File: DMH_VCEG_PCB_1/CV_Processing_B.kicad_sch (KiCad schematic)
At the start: 58 parts, among them J26 Conn_01x10_PinHeader, Q27 BC558, Q28 BC558, Q29 BC548, Q30 BC548, Q31 BC548, Q32 BC548, U18 TL074, U19 TL074, U20 TL074

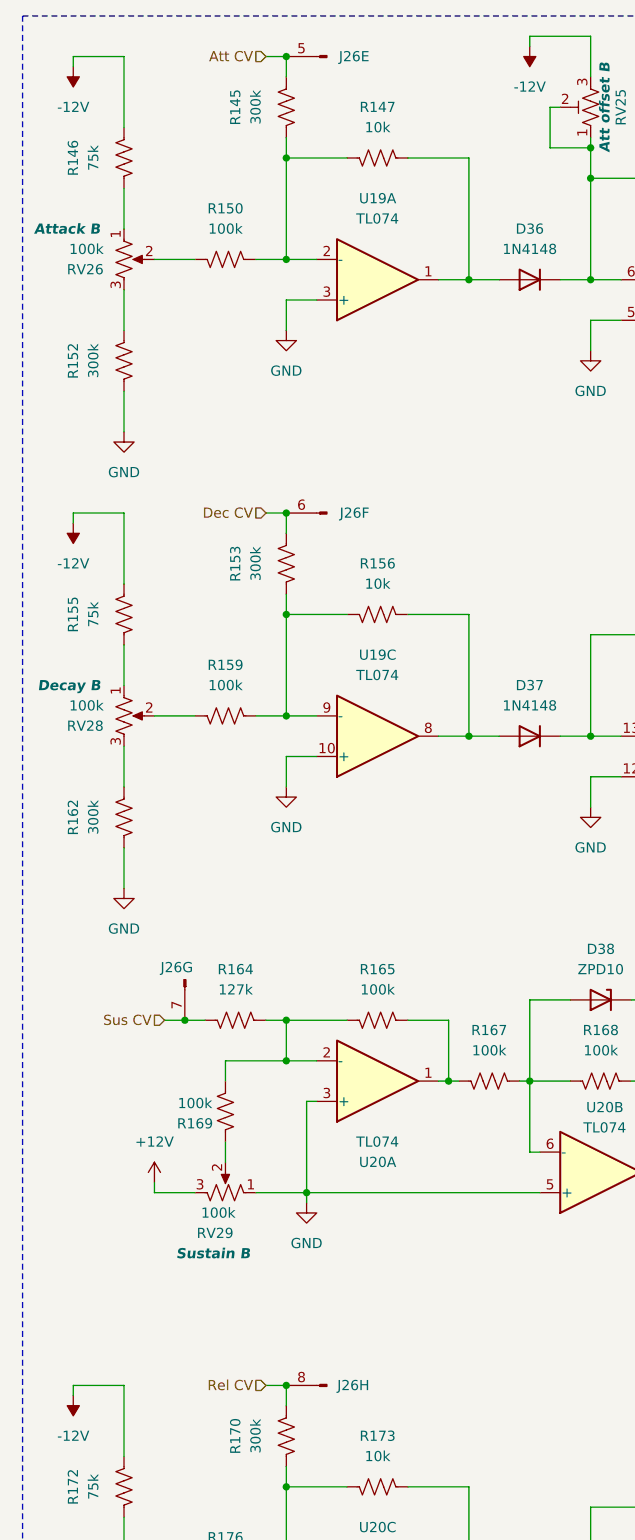
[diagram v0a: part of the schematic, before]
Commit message: PCB 2 placement in progress
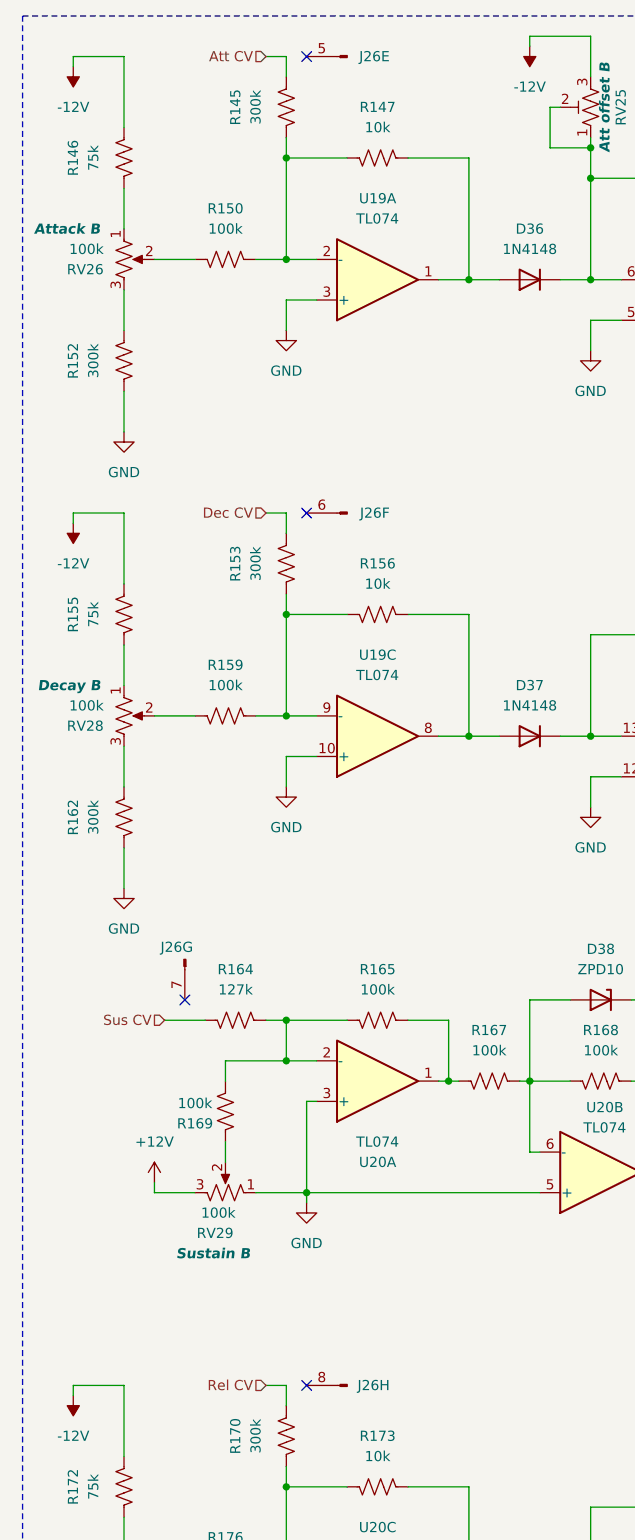
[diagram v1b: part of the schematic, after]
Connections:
- net Att CV: no longer J26.5 (Pin_5)
- net Dec CV: no longer J26.6 (Pin_6)
- net Rel CV: no longer J26.8 (Pin_8)
- net Sus CV: no longer J26.7 (Pin_7)
- no-connect marks 0 -> 4

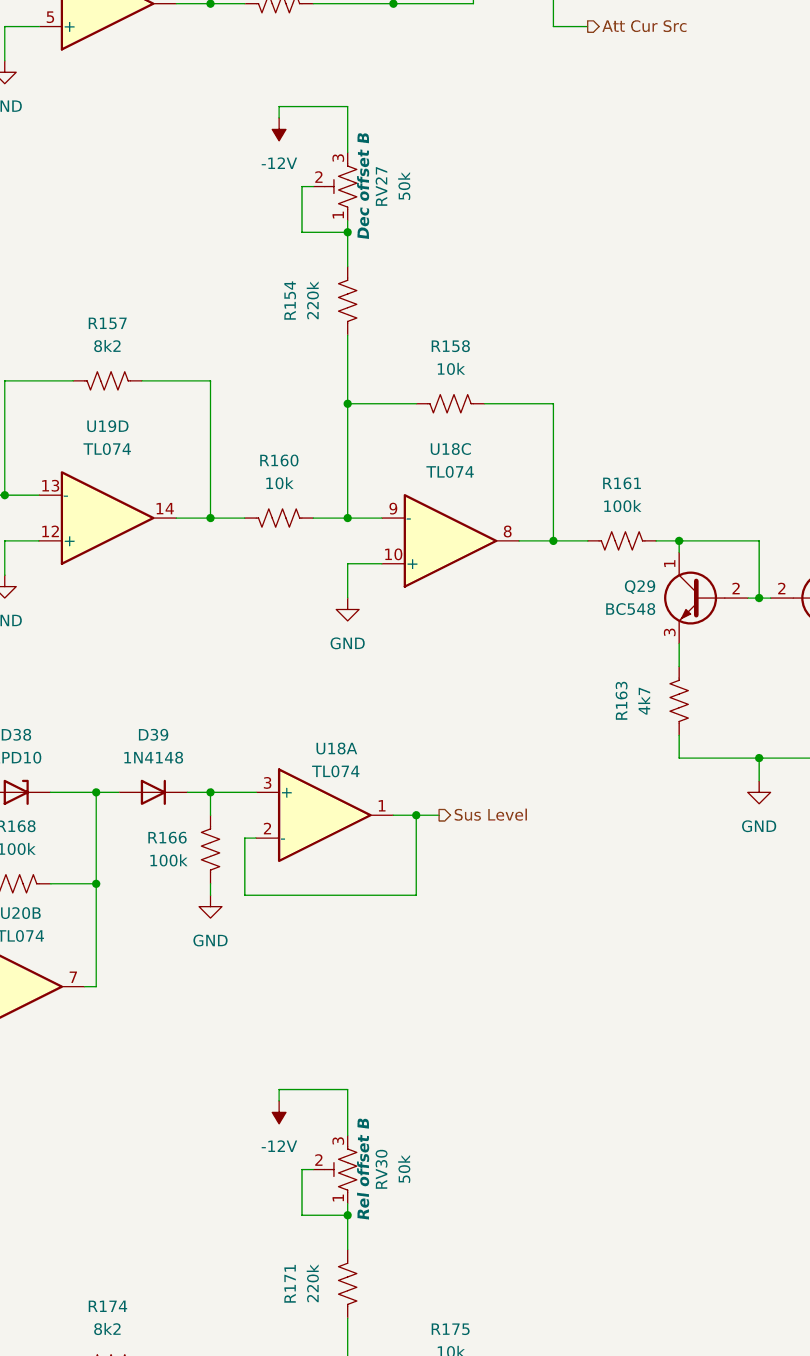
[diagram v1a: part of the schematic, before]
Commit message: Updated Dec and Rel trimpots to 100k
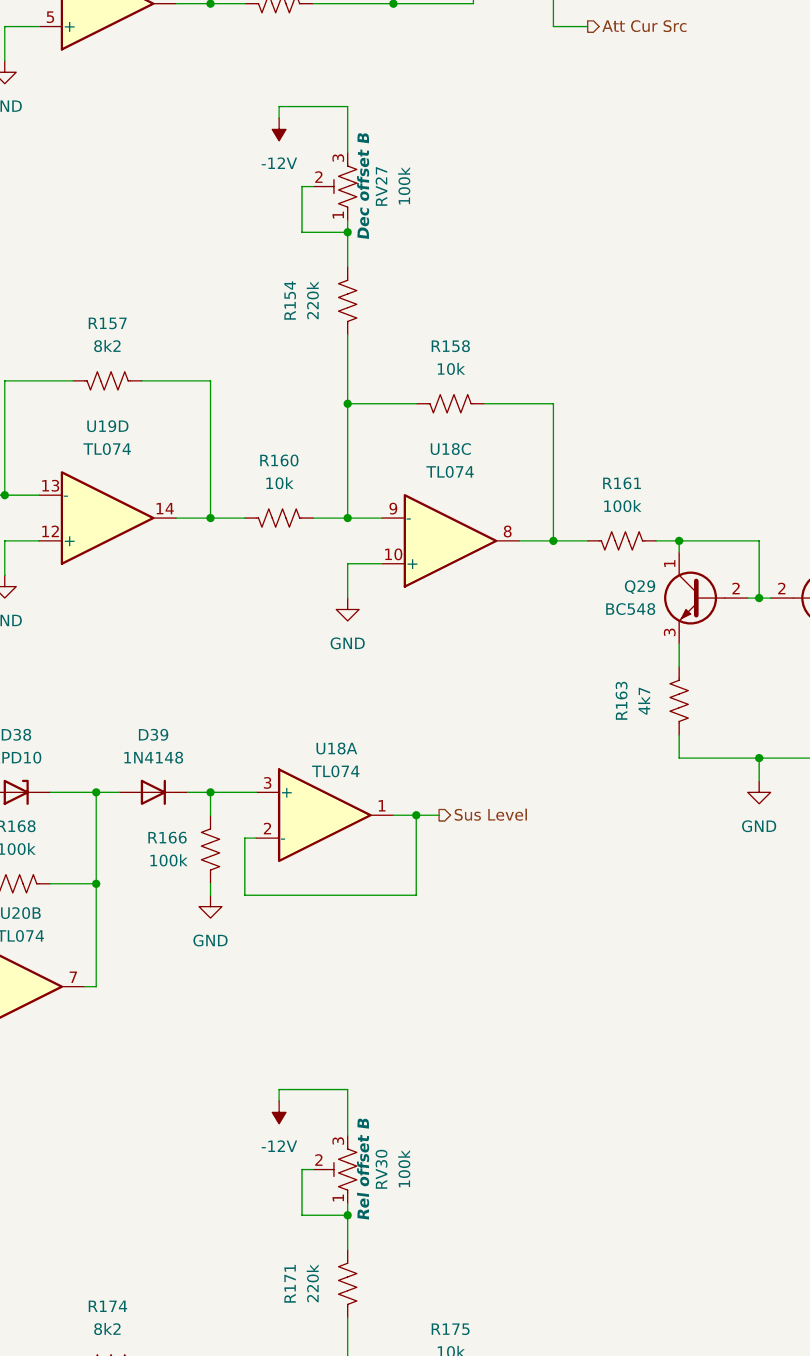
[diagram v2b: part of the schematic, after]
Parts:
- RV27, RV30: value 50k -> 100k
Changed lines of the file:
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@@
 			)
 		)
-		(property "Value" "50k"
+		(property "Value" "100k"
 			(at 128.27 69.85 90)
 			(effects
@@
 			)
 		)
-		(property "Value" "50k"
+		(property "Value" "100k"
 			(at 128.27 179.07 90)
 			(effects

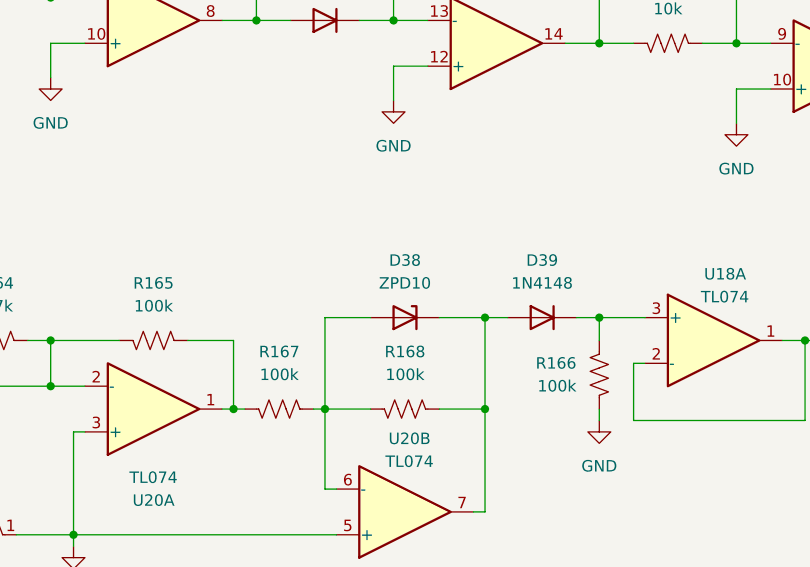
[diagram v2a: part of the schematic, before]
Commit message: PCB 2 placement ongoing
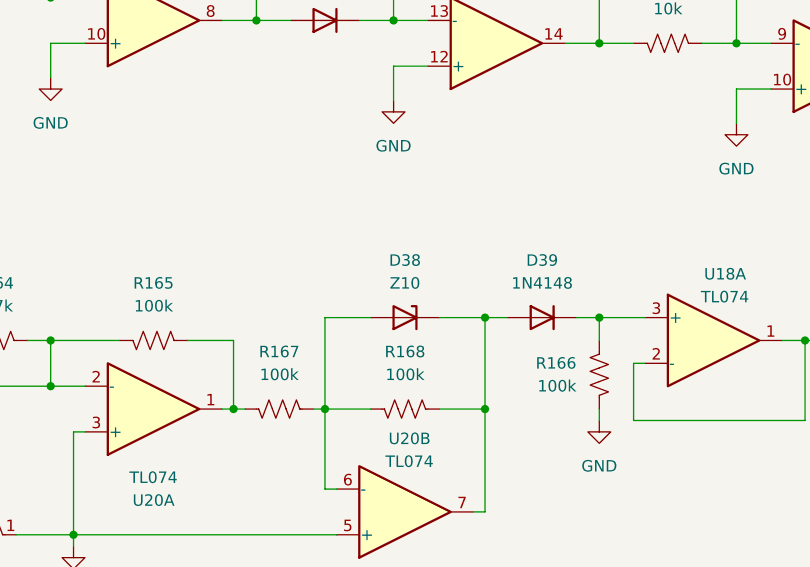
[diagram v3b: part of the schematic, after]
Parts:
- D38: value ZPD10 -> Z10
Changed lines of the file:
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@@
 			)
 		)
-		(property "Value" "ZPD10"
+		(property "Value" "Z10"
 			(at 85.09 133.35 0)
 			(effects

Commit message: PCB 2 routing in progress
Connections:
- net Att CV: now also J26.5 (Pin_5)
- net Dec CV: now also J26.6 (Pin_6)
- net Rel CV: now also J26.8 (Pin_8)
- net Sus CV: now also J26.7 (Pin_7)
- no-connect marks 4 -> 0
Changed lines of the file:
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@@
+	)
+	(junction
+		(at 45.72 76.2)
+		(diameter 0)
+		(color 0 0 0 0)
 	)
 	(junction
@@
 	)
 	(junction
+		(at 45.72 19.05)
+		(diameter 0)
+		(color 0 0 0 0)
+	)
+	(junction
 		(at 121.92 215.9)
 		(diameter 0)
@@
 	)
 	(junction
+		(at 33.02 139.7)
+		(diameter 0)
+		(color 0 0 0 0)
+	)
+	(junction
 		(at 106.68 137.16)
 		(diameter 0)
@@
 	)
 	(junction
+		(at 45.72 185.42)
+		(diameter 0)
+		(color 0 0 0 0)
+	)
+	(junction
 		(at 127 49.53)
 		(diameter 0)
@@
 		(color 0 0 0 0)
 	)
-	(no_connect
-		(at 48.26 185.42)
-	)
-	(no_connect
-		(at 48.26 76.2)
-	)
-	(no_connect
-		(at 33.02 137.16)
-	)
-	(no_connect
-		(at 48.26 19.05)
-	)
 	(wire
 		(pts
@@
 	(wire
 		(pts
-			(xy 30.48 139.7) (xy 35.56 139.7)
+			(xy 30.48 139.7) (xy 33.02 139.7)
 		)
 		(stroke
@@
 	(wire
 		(pts
+			(xy 45.72 19.05) (xy 48.26 19.05)
+		)
+		(stroke
+			(width 0)
+			(type default)
+		)
+	)
+	(wire
+		(pts
 			(xy 121.92 170.18) (xy 121.92 175.26)
 		)
@@
 	(wire
 		(pts
+			(xy 33.02 137.16) (xy 33.02 139.7)
+		)
+		(stroke
+			(width 0)
+			(type default)
+		)
+	)
+	(wire
+		(pts
 			(xy 102.87 215.9) (xy 106.68 215.9)
 		)
@@
 	(wire
 		(pts
+			(xy 45.72 185.42) (xy 48.26 185.42)
+		)
+		(stroke
+			(width 0)
+			(type default)
+		)
+	)
+	(wire
+		(pts
 			(xy 176.53 120.65) (xy 176.53 133.35)
 		)
@@
 	(wire
 		(pts
+			(xy 45.72 76.2) (xy 48.26 76.2)
+		)
+		(stroke
+			(width 0)
+			(type default)
+		)
+	)
+	(wire
+		(pts
 			(xy 80.01 104.14) (xy 83.82 104.14)
 		)
@@
 		)
 		(stroke
+			(width 0)
+			(type default)
+		)
+	)
+	(wire
+		(pts
+			(xy 33.02 139.7) (xy 35.56 139.7)
+		)
+		(stroke

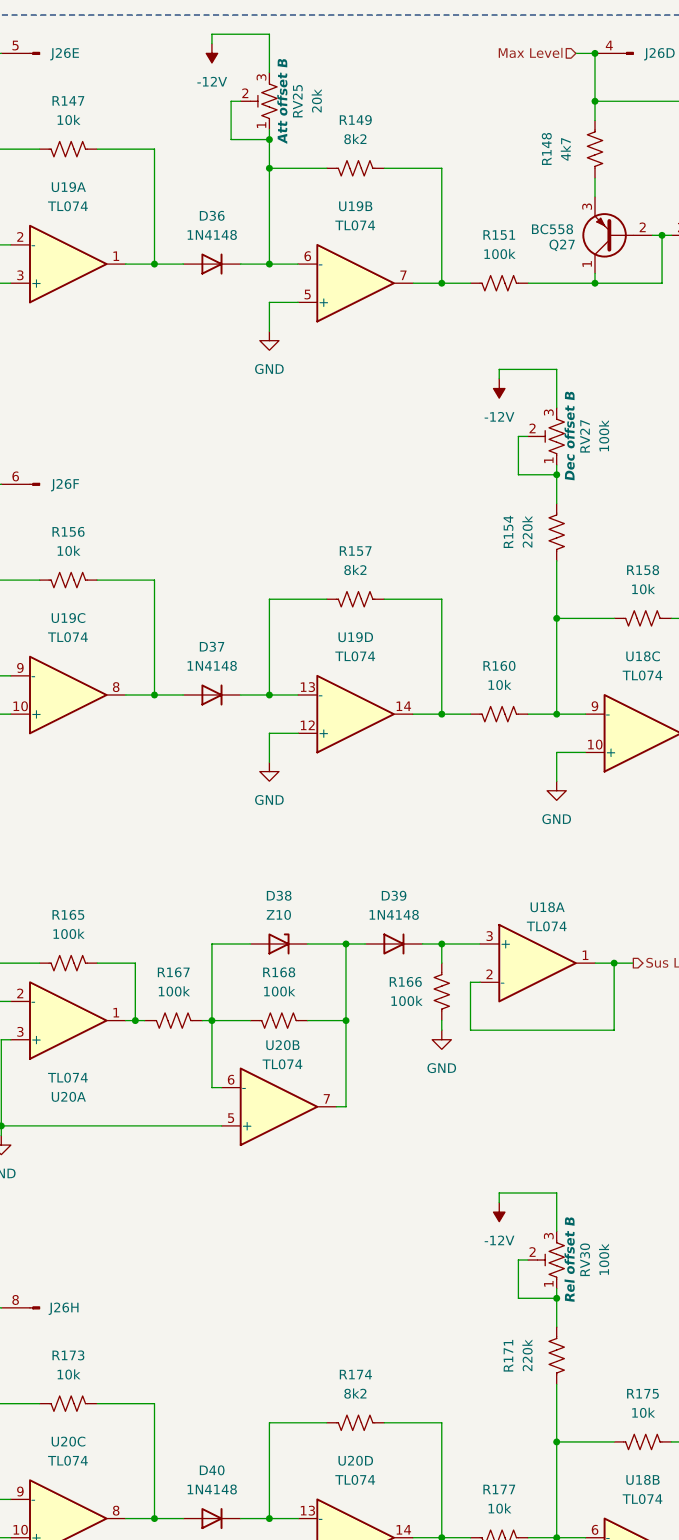
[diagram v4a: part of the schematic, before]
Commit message: Updated PCB 1 with changes from breadboard tests
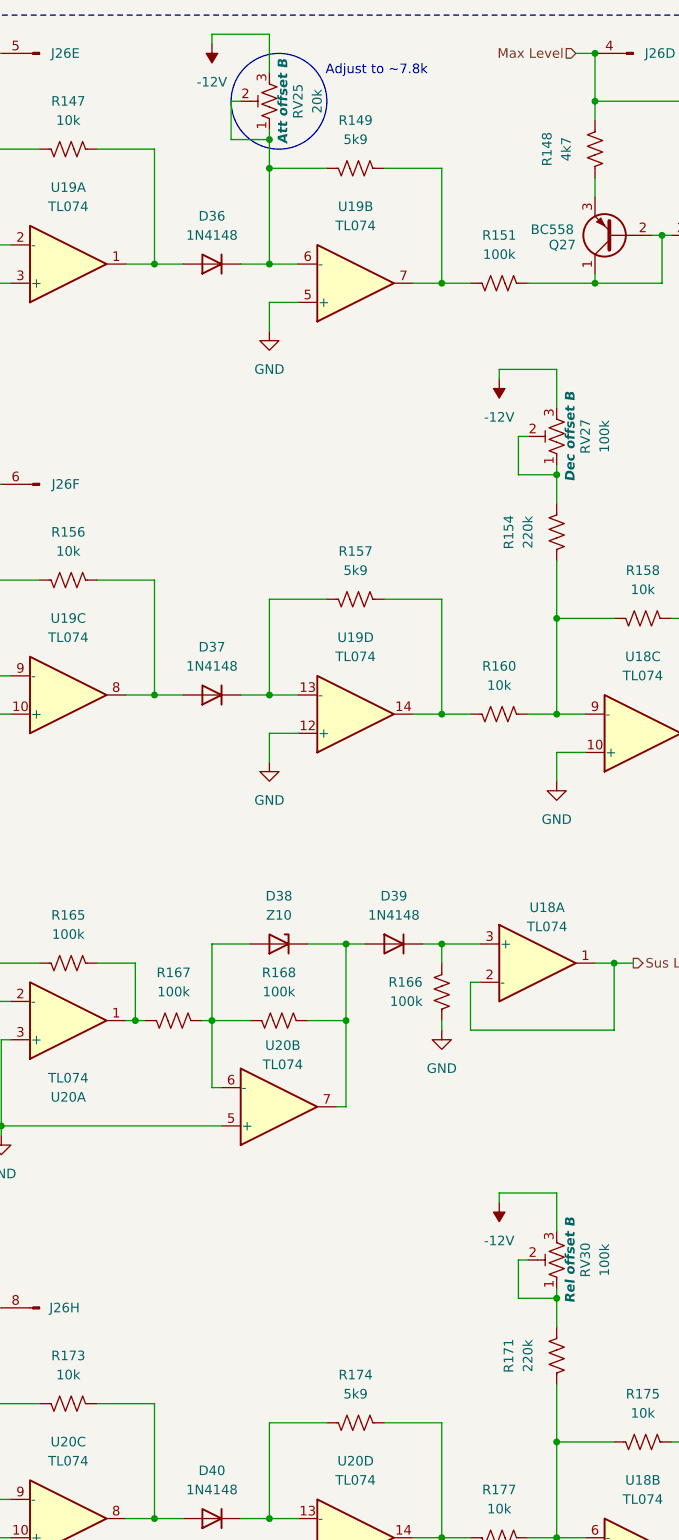
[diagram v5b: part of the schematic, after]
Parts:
- R149, R157, R174: value 8k2 -> 5k9
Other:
- note added: "Adjust to ~7.8k"
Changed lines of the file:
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@@
 		)
 	)
+	(circle
+		(center 85.09 25.4)
+		(radius 6.35)
+		(stroke
+			(width 0)
+			(type default)
+		)
+		(fill
+			(type none)
+		)
+	)
+	(text "Adjust to ~7.8k"
+		(exclude_from_sim no)
+		(at 98.044 21.336 0)
+		(effects
+			(font
+				(size 1.27 1.27)
+			)
+		)
+	)
 	(text "PCB 2"
 		(exclude_from_sim no)
@@
 			)
 		)
-		(property "Value" "8k2"
+		(property "Value" "5k9"
 			(at 95.25 87.63 90)
 			(effects
@@
 			)
 		)
-		(property "Value" "8k2"
+		(property "Value" "5k9"
 			(at 95.25 196.85 90)
 			(effects
@@
 			)
 		)
-		(property "Value" "8k2"
+		(property "Value" "5k9"
 			(at 95.25 30.48 90)
 			(effects
